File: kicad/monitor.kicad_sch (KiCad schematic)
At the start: 5 parts, among them SW3 SW_DPDT_x2, U12 NE5532

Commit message: phones out
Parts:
- removed R72, R73, R74: 10k, symbol Device:R_US
- removed SW3: SW_DPDT_x2, symbol openmic:SW_DPDT_x2
- removed U12: NE5532, symbol Amplifier_Operational:NE5532
- added C39, C40: 0.01uF, symbol Device:C
- added C41: 100uF, symbol Device:C_Polarized_US
- added C42, C43, C44, C45, C46, C47, C48, C49, C50, C51, C52, C53: 100nF, symbol Device:C_Small
- added D1, D13, D40, D41, D42, D43, D44, D45, D46, D47, D48, D7: WS2812B-2020, LED_SMD:LED_WS2812B-2020_PLCC4_2.0x2.0mm, symbol LED:WS2812B-2020
- added R57, R58, R59, R60: 10k, symbol Device:R_US
- added SW3: RotaryEncoder, symbol Device:RotaryEncoder
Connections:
- new net: D47.1 (DOUT), D48.3 (DIN)
- new net: D42.1 (DOUT), D43.3 (DIN)
- new net: D41.1 (DOUT), D42.3 (DIN)
- new net: D46.1 (DOUT), D47.3 (DIN)
- new net: D45.1 (DOUT), D46.3 (DIN)
- new net: D43.1 (DOUT), D44.3 (DIN)
- new net: C40.1, R59.2, R60.1, SW3.B
- new net: C39.1, R57.2, R58.1, SW3.A
- new net: D44.1 (DOUT), D45.3 (DIN)
- new net: D13.1 (DOUT), D40.3 (DIN)
- new net: D13.3 (DIN), D7.1 (DOUT)
- new net: D40.1 (DOUT), D41.3 (DIN)
- new net: D1.1 (DOUT), D7.3 (DIN)
- new net +3V3: R58.2, R59.1
- new net +5V: C41.1, C42.1, C43.1, C44.1, C45.1, C46.1, C47.1, C48.1, C49.1, C50.1, C51.1, C52.1, C53.1, D1.4 (VDD), D13.4 (VDD), D40.4 (VDD), D41.4 (VDD), D42.4 (VDD), D43.4 (VDD), D44.4 (VDD), D45.4 (VDD), D46.4 (VDD), D47.4 (VDD), D48.4 (VDD), D7.4 (VDD)
- new net GNDD: C39.2, C40.2, C41.2, C42.2, C43.2, C44.2, C45.2, C46.2, C47.2, C48.2, C49.2, C50.2, C51.2, C52.2, C53.2, D1.2 (VSS), D13.2 (VSS), D40.2 (VSS), D41.2 (VSS), D42.2 (VSS), D43.2 (VSS), D44.2 (VSS), D45.2 (VSS), D46.2 (VSS), D47.2 (VSS), D48.2 (VSS), D7.2 (VSS), SW3.C
- new net LED_DIN: D1.3 (DIN)
- new net LED_DOUT: D48.1 (DOUT)
- new net ROT_A: R57.1
- new net ROT_B: R60.2
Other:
- note added: "direct monitor knob"
- note removed: "direct monitor switch"

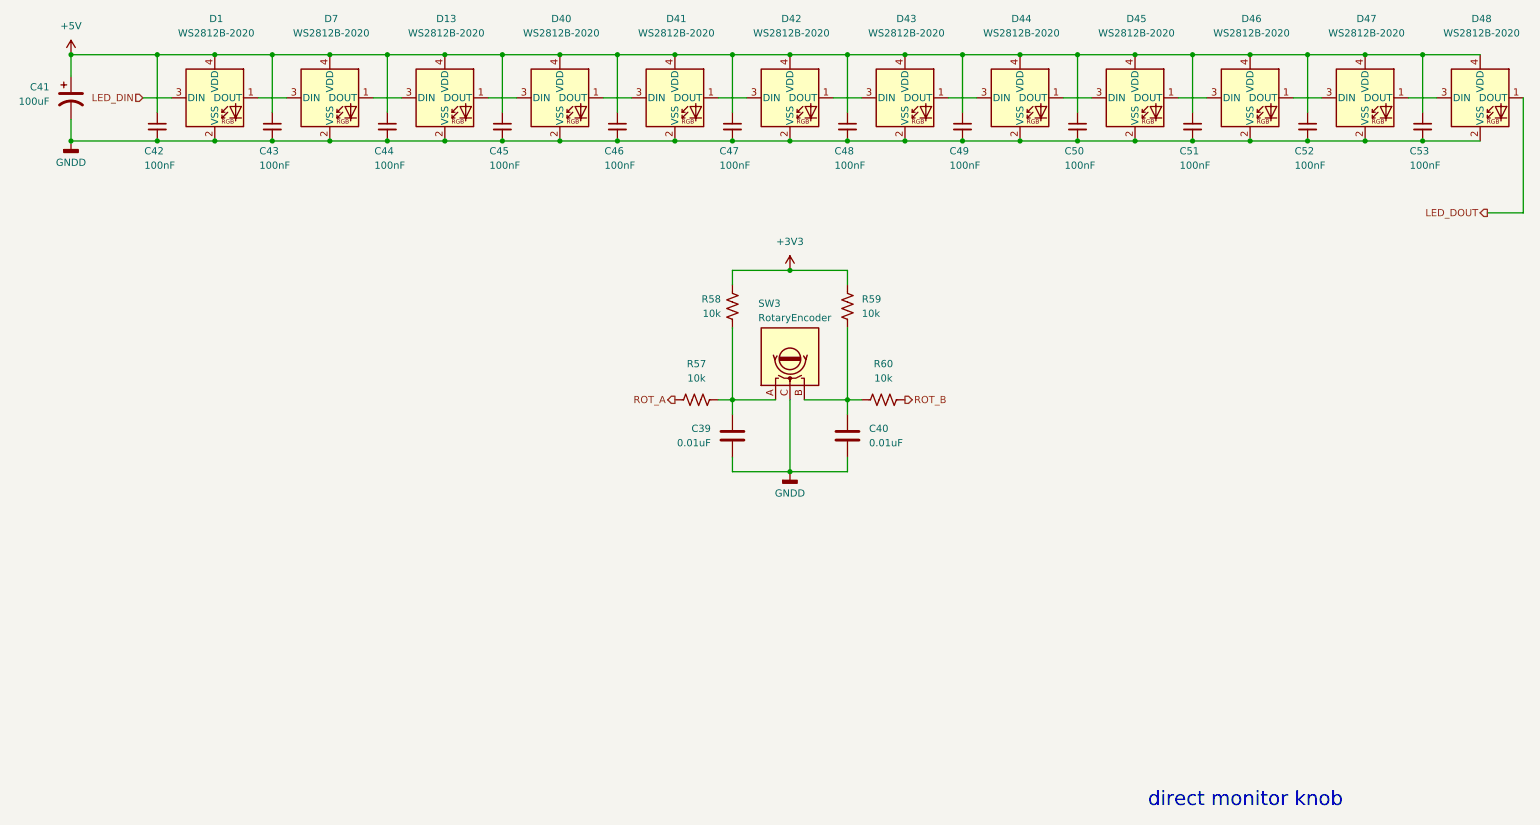
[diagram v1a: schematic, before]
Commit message: monitor switch
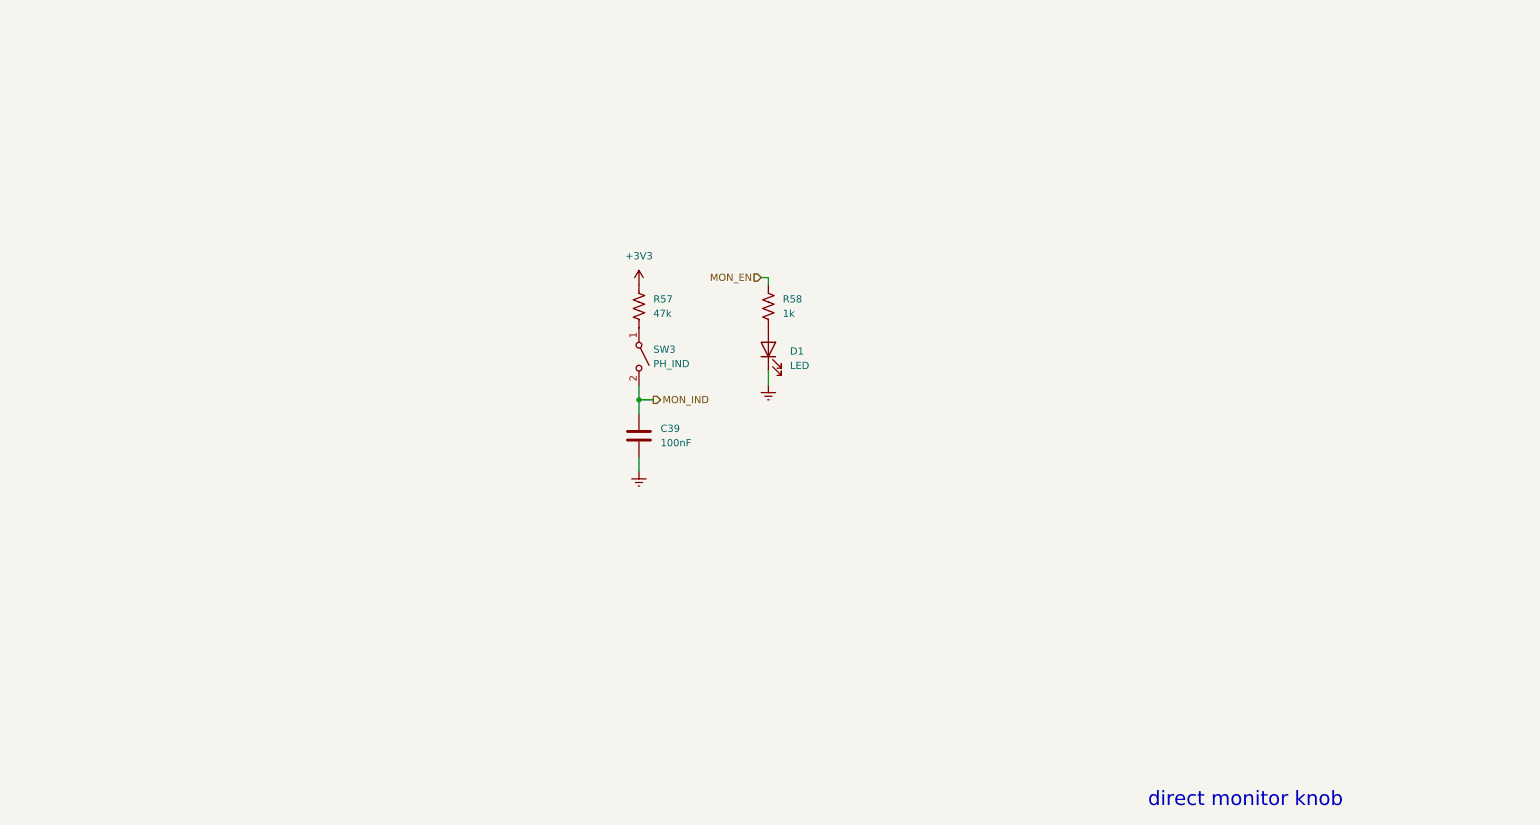
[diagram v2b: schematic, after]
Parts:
- removed C40: 0.01uF, symbol Device:C
- removed C41: 100uF, symbol Device:C_Polarized_US
- removed C42, C43, C44, C45, C46, C47, C48, C49, C50, C51, C52, C53: 100nF, symbol Device:C_Small
- removed D1, D13, D40, D41, D42, D43, D44, D45, D46, D47, D48, D7: WS2812B-2020, LED_SMD:LED_WS2812B-2020_PLCC4_2.0x2.0mm, symbol LED:WS2812B-2020
- removed R59, R60: 10k, symbol Device:R_US
- removed SW3: RotaryEncoder, symbol Device:RotaryEncoder
- added D1: LED, symbol Device:LED
- added SW3: PH_IND, symbol Switch:SW_SPST
- C39: value 0.01uF -> 100nF
- R57: value 10k -> 47k
- R58: value 10k -> 1k
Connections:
- net ROT_A is gone; now on net +3V3: R57.1
- net +3V3: no longer R58.2
- net GNDD renamed Earth
- net Earth: now also D1.1 (K)
- new net: D1.2 (A), R58.2
- new net: R57.2, SW3.1 (A)
- new net MON_EN: R58.1
- new net MON_IND: C39.1, SW3.2 (B)

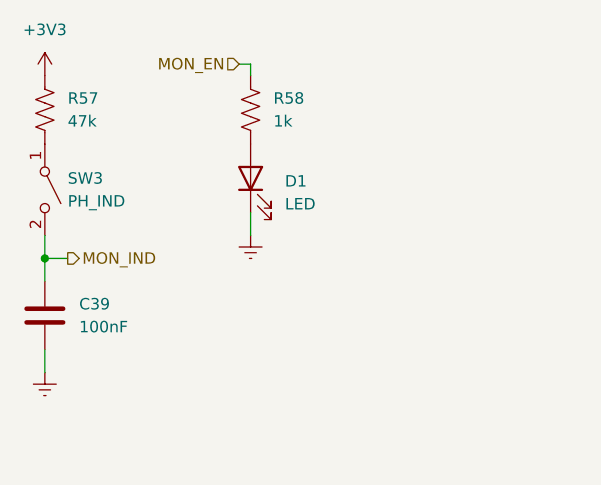
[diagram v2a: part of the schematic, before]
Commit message: CH224K external supply
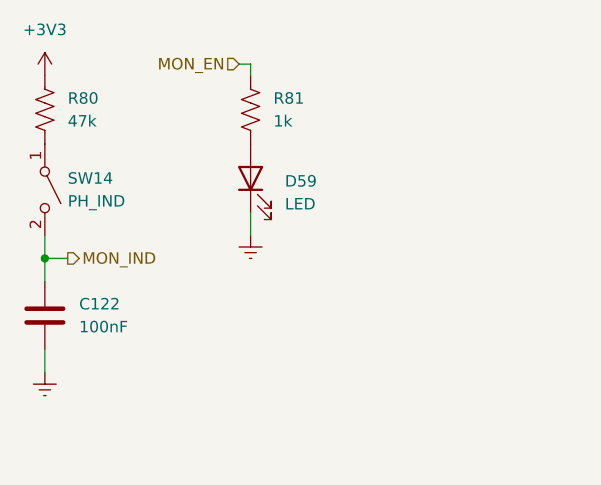
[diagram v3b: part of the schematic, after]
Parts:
- renumbered C39 to C122, D1 to D59, R57 to R80, R58 to R81, SW3 to SW14
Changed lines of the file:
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@@
 		(dnp no)
 		(fields_autoplaced yes)
-		(property "Reference" "R58"
+		(property "Reference" "R81"
 			(at 148.59 85.0899 0)
 			(effects
@@
 			(project "openmic"
 				(path "/84faeadc-8b12-4a66-a17f-5c56e5923fb8/96971848-86f2-4431-9c99-2e7a6e65db3c"
-					(reference "R58")
+					(reference "R81")
 					(unit 1)
 				)
@@
 		(dnp no)
 		(fields_autoplaced yes)
-		(property "Reference" "R57"
+		(property "Reference" "R80"
 			(at 125.73 85.0899 0)
 			(effects
@@
 			(project "openmic"
 				(path "/84faeadc-8b12-4a66-a17f-5c56e5923fb8/96971848-86f2-4431-9c99-2e7a6e65db3c"
-					(reference "R57")
+					(reference "R80")
 					(unit 1)
 				)
@@
 		(dnp no)
 		(fields_autoplaced yes)
-		(property "Reference" "#PWR074"
+		(property "Reference" "#PWR0143"
 			(at 146.05 106.68 0)
 			(effects
@@
 			(project "openmic"
 				(path "/84faeadc-8b12-4a66-a17f-5c56e5923fb8/96971848-86f2-4431-9c99-2e7a6e65db3c"
-					(reference "#PWR074")
+					(reference "#PWR0143")
 					(unit 1)
 				)
@@
 		(dnp no)
 		(fields_autoplaced yes)
-		(property "Reference" "C39"
+		(property "Reference" "C122"
 			(at 127 107.9499 0)
 			(effects
@@
 			(project "openmic"
 				(path "/84faeadc-8b12-4a66-a17f-5c56e5923fb8/96971848-86f2-4431-9c99-2e7a6e65db3c"
-					(reference "C39")
+					(reference "C122")
 					(unit 1)
 				)
@@
 		(dnp no)
 		(fields_autoplaced yes)
-		(property "Reference" "#PWR070"
+		(property "Reference" "#PWR0141"
 			(at 123.19 86.36 0)
 			(effects
@@
 			(project "openmic"
 				(path "/84faeadc-8b12-4a66-a17f-5c56e5923fb8/96971848-86f2-4431-9c99-2e7a6e65db3c"
-					(reference "#PWR070")
+					(reference "#PWR0141")
 					(unit 1)
 				)
@@
 		(dnp no)
 		(fields_autoplaced yes)
-		(property "Reference" "SW3"
+		(property "Reference" "SW14"
 			(at 125.73 93.9799 90)
 			(effects
@@
 			(project "openmic"
 				(path "/84faeadc-8b12-4a66-a17f-5c56e5923fb8/96971848-86f2-4431-9c99-2e7a6e65db3c"
-					(reference "SW3")
+					(reference "SW14")
 					(unit 1)
 				)
@@
 		(dnp no)
 		(fields_autoplaced yes)
-		(property "Reference" "#PWR073"
+		(property "Reference" "#PWR0148"
 			(at 123.19 121.92 0)
 			(effects
@@
 			(project "openmic"
 				(path "/84faeadc-8b12-4a66-a17f-5c56e5923fb8/96971848-86f2-4431-9c99-2e7a6e65db3c"
-					(reference "#PWR073")
+					(reference "#PWR0148")
 					(unit 1)
 				)
@@
 		(dnp no)
 		(fields_autoplaced yes)
-		(property "Reference" "D1"
+		(property "Reference" "D59"
 			(at 149.86 94.2974 90)
 			(effects
@@
 			(project "openmic"
 				(path "/84faeadc-8b12-4a66-a17f-5c56e5923fb8/96971848-86f2-4431-9c99-2e7a6e65db3c"
-					(reference "D1")
-					(unit 1)
-				)
+					(reference "D59")
+					(unit 1)
+				)
